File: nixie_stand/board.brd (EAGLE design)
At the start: 25 x 30 mm, 2 parts

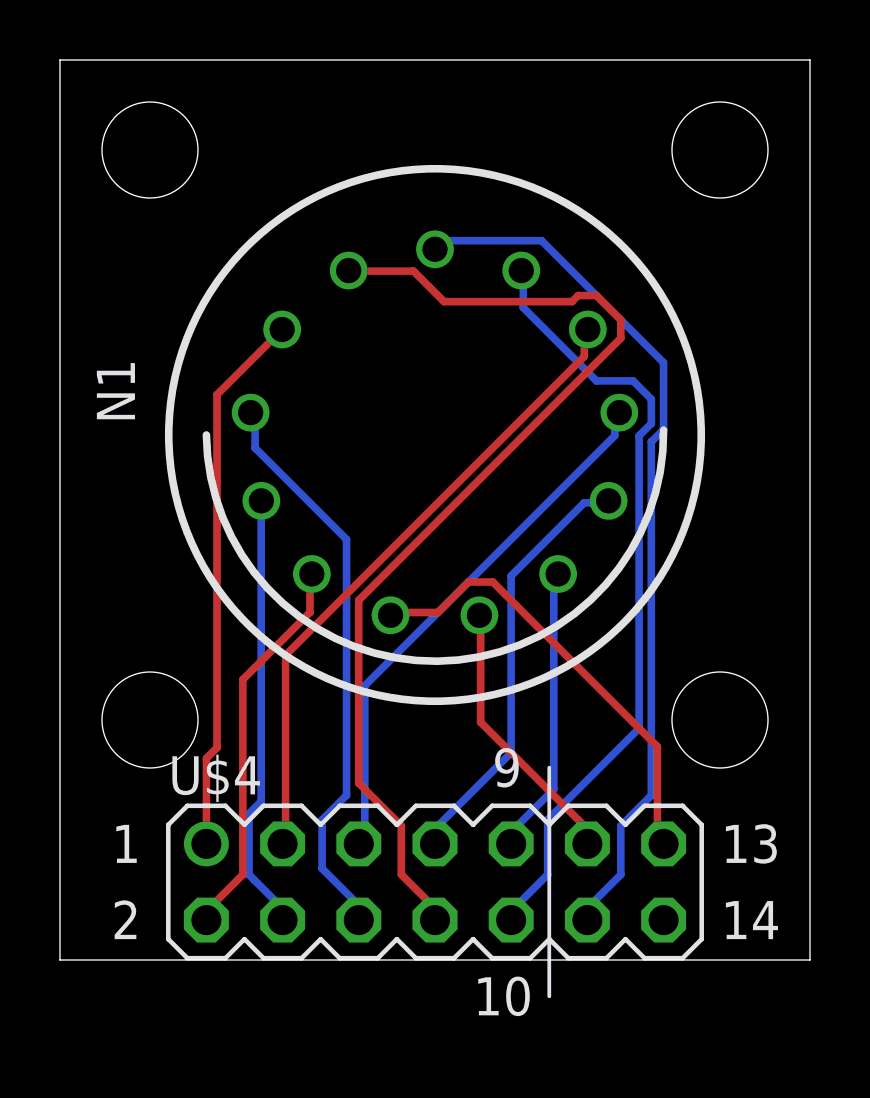
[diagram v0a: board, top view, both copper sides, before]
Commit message: [fix] 太さ・ガーバー出力(FusionPCB)
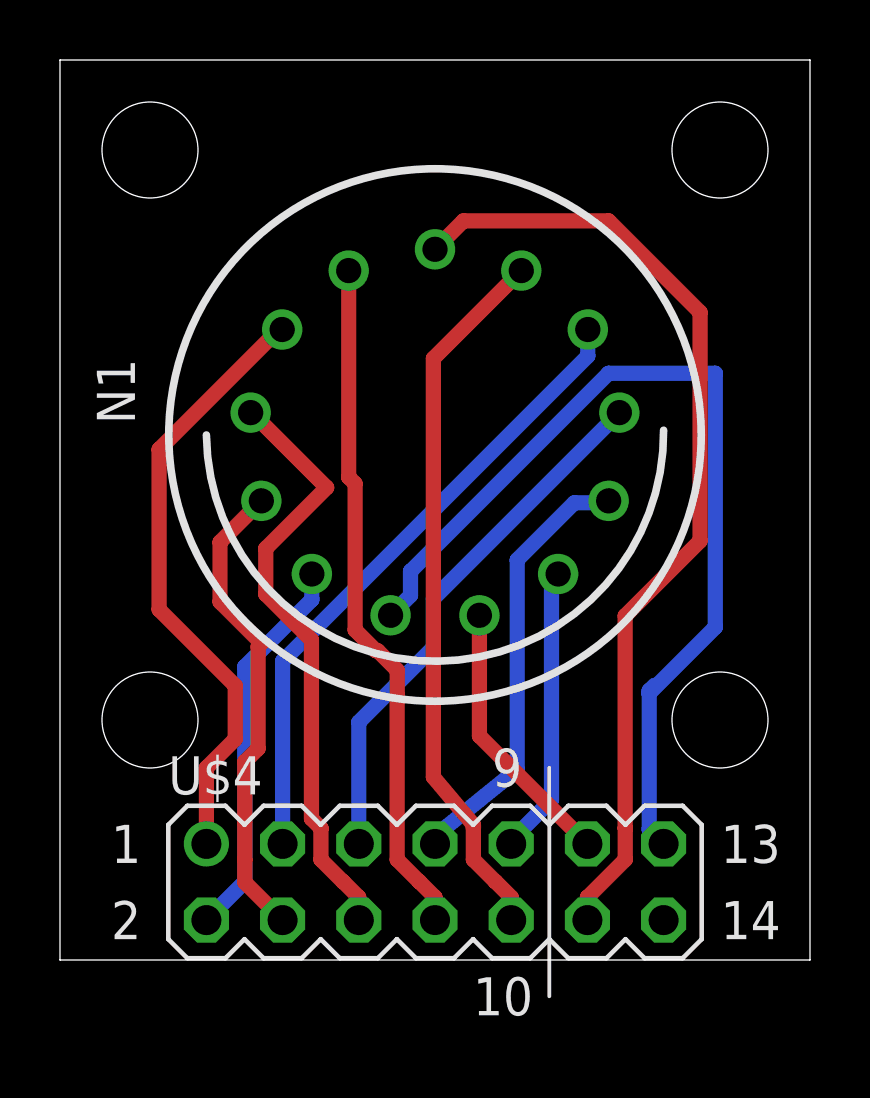
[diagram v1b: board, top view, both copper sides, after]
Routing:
- net NIXIE6: track 14.9 -> 31.8 mm
- net N$2: track 34.6 -> 22.9 mm
- net N$1: track 29.1 -> 33.1 mm
- net N$3: track 26.1 -> 23.9 mm
- net NIXIE0: track 18.3 -> 20.3 mm
- net NIXIE8: track 14.6 -> 15.9 mm
- net NIXIE9: track 19.1 -> 20.1 mm
